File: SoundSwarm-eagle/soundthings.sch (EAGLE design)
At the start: 34 parts, among them Q1 IRLIB9343PbF, Q2 IRLB8721PBF, Q4 IRLB8721PBF

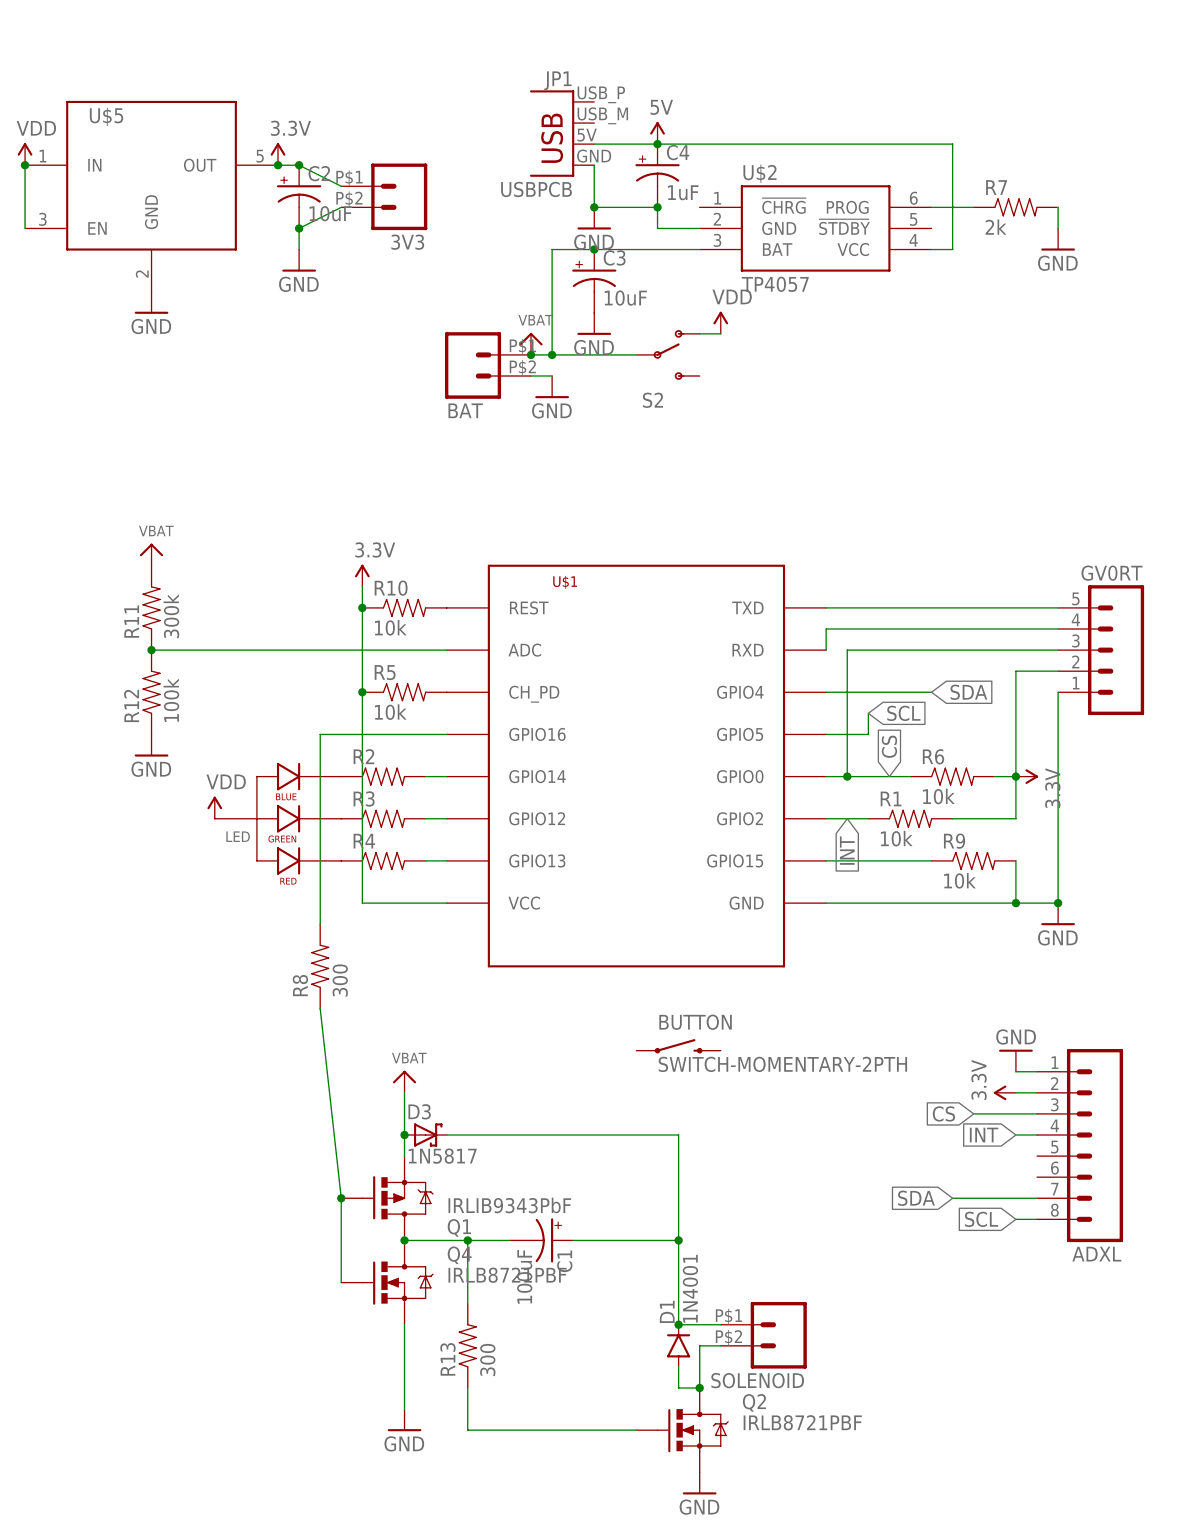
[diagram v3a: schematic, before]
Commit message: New schematic using DC-DC converter; needs Eagle-Lio-Library
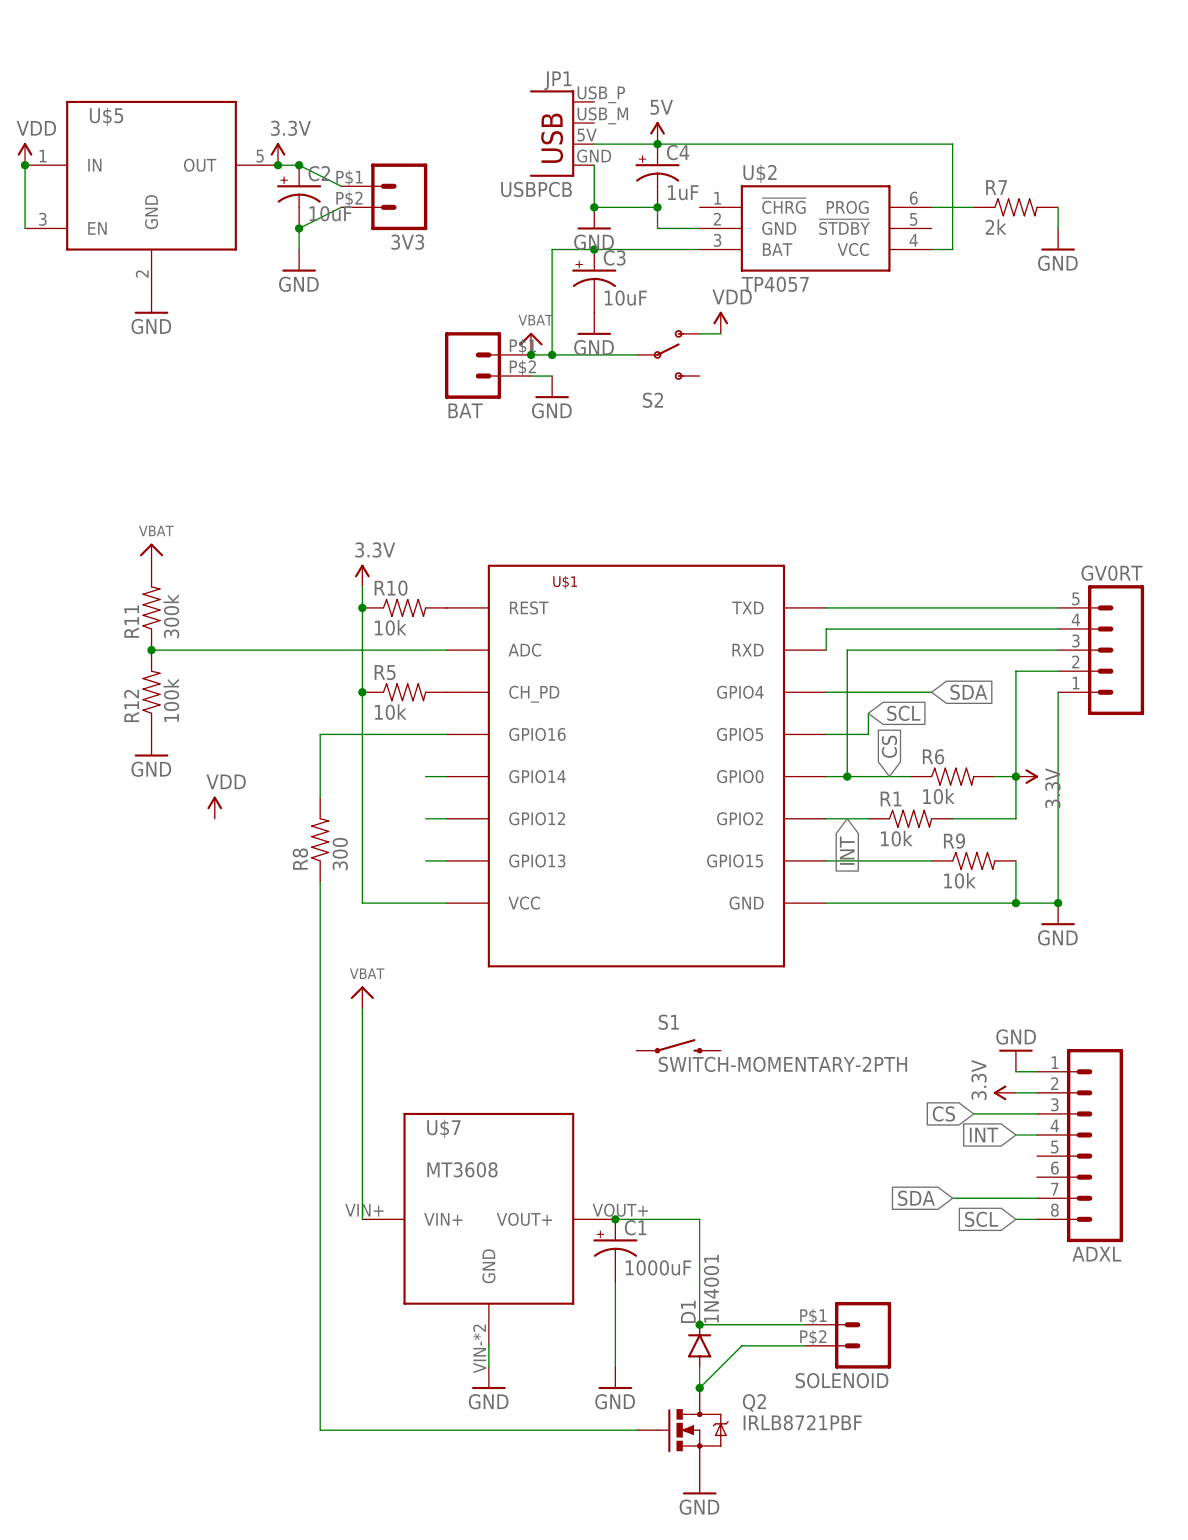
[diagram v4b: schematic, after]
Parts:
- removed D3: 1N5817, adafruit:SCHOTTKY-DIODEDO41
- removed LED: LED-RGB-CA-THRUCLEAR, SparkFun-LED:LED-RGB-CA-THRUCLEAR
- removed Q1: IRLIB9343PbF, SparkFun-DiscreteSemi:MOSFET-PCHANNELFQP27P06
- removed Q4: IRLB8721PBF, SparkFun-DiscreteSemi:MOSFET-NCHANNELFQP30N06L
- removed R13: 300, SparkFun-Passives:RESISTORAXIAL-0.3
- removed R2, R3, R4: (no value), SparkFun-Passives:RESISTORAXIAL-0.3
- added U$7: MT3608, lio:MT3608
- C1: value 100uF -> 1000uF
- renumbered BUTTON to S1
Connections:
- removed net N$12: Q2.G, R13.1
- removed net N$14: LED.RED_CATHODE, R4.1
- removed net N$2: LED.BLUE_CATHODE, R2.1
- removed net N$4: C1.-, Q1.D, Q4.D, R13.2
- removed net N$9: LED.GREEN_CATHODE, R3.1
- removed net VHI: C1.+, D1.C, D3.C, SOLENOID.1
- new net VOUT+: C1.+, D1.C, SOLENOID.1, U$7.VOUT+
- net GATE: now also Q2.G; no longer Q1.G, Q4.G
- net GND: now also C1.-, U$7.GND; no longer Q4.S
- net N$5: no longer R4.2
- net N$6: no longer R3.2
- net N$7: no longer R2.2
- net VBAT: now also U$7.VIN+; no longer D3.A, Q1.S
- net VDD: no longer LED.ANODE
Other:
- moved on the sheet: C1, D1, R8, SOLENOID

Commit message: Fixed PCB layout v2
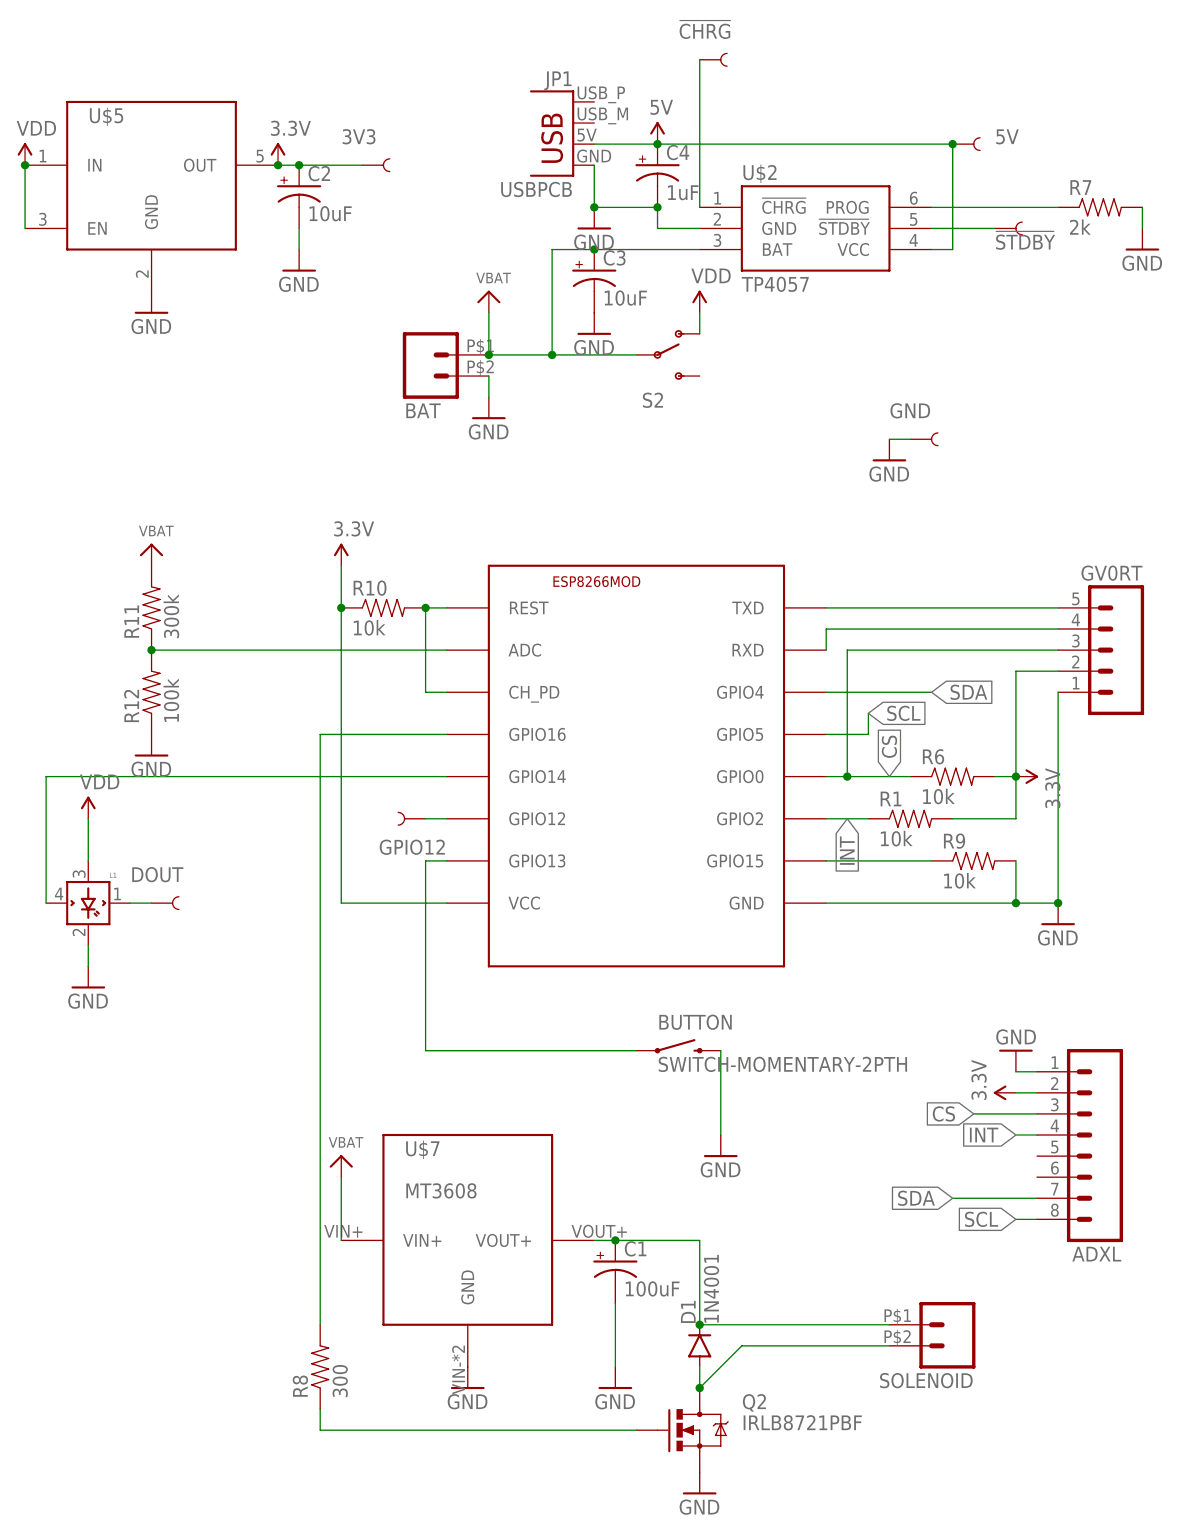
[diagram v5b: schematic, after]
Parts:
- removed R5: 10k, SparkFun-Passives:RESISTORAXIAL-0.3
- added !CHRG, !STDBY, 5V, DOUT, GND, GPIO12: TEST-POINTTP_15TH_THRU, SparkFun-Passives:TEST-POINTTP_15TH_THRU
- added L1: WS2812BTH, lio:WS2812BTH
- 3V3: value (none) -> TEST-POINTTP_15TH_THRU; device SparkFun-Connectors:M02PTH2 -> SparkFun-Passives:TEST-POINTTP_15TH_THRU
- C1: value 1000uF -> 100uF
- renumbered S1 to BUTTON, U$1 to ESP8266MOD
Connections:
- net N$1 renamed SOL-
- net N$15 renamed TX
- net N$16 renamed RX
- net N$19 renamed GPIO15
- removed net N$20: ESP8266MOD.REST, R10.2
- removed net N$5: ESP8266MOD.GPIO13
- removed net N$7: ESP8266MOD.GPIO14
- new net DIN: ESP8266MOD.GPIO14, L1.DIN
- new net DOUT: DOUT.1, L1.DOUT
- new net EN: ESP8266MOD.CH_PD, ESP8266MOD.REST, R10.2
- new net GPIO13: BUTTON.1, ESP8266MOD.GPIO13
- new net N$8: !CHRG.1, U$2.!CHRG
- net 3.3V: no longer R5.1
- net 5V: now also 5V.1
- net GND: now also BUTTON.2, GND.1, L1.GND; no longer 3V3.2
- net N$3: now also !STDBY.1, U$2.!STDBY; no longer ESP8266MOD.CH_PD, R5.2
- net N$6: now also GPIO12.1
- net VDD: now also L1.VDD
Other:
- moved on the sheet: BAT, C1, R10, R7, R8, SOLENOID, U$7

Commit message: Move away from the edges; add labels
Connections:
- net N$3 renamed !STDBY
- net N$6 renamed GPIO12
- net N$8 renamed !CHRG
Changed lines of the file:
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@@
 <grid distance="0.1" unitdist="inch" unit="inch" style="lines" multiple="1" display="no" altdistance="0.01" altunitdist="inch" altunit="inch"/>
 <layers>
-<layer number="1" name="Top" color="4" fill="1" visible="yes" active="no"/>
-<layer number="16" name="Bottom" color="1" fill="1" visible="yes" active="no"/>
-<layer number="17" name="Pads" color="2" fill="1" visible="yes" active="no"/>
-<layer number="18" name="Vias" color="2" fill="1" visible="yes" active="no"/>
-<layer number="19" name="Unrouted" color="6" fill="1" visible="yes" active="no"/>
-<layer number="20" name="Dimension" color="15" fill="1" visible="yes" active="no"/>
-<layer number="21" name="tPlace" color="7" fill="1" visible="yes" active="no"/>
-<layer number="22" name="bPlace" color="7" fill="1" visible="yes" active="no"/>
-<layer number="23" name="tOrigins" color="15" fill="1" visible="yes" active="no"/>
-<layer number="24" name="bOrigins" color="15" fill="1" visible="yes" active="no"/>
-<layer number="25" name="tNames" color="7" fill="1" visible="yes" active="no"/>
-<layer number="26" name="bNames" color="7" fill="1" visible="yes" active="no"/>
-<layer number="27" name="tValues" color="7" fill="1" visible="yes" active="no"/>
-<layer number="28" name="bValues" color="7" fill="1" visible="yes" active="no"/>
+<layer number="1" name="Top" color="4" fill="1" visible="no" active="no"/>
+<layer number="16" name="Bottom" color="1" fill="1" visible="no" active="no"/>
+<layer number="17" name="Pads" color="2" fill="1" visible="no" active="no"/>
+<layer number="18" name="Vias" color="2" fill="1" visible="no" active="no"/>
+<layer number="19" name="Unrouted" color="6" fill="1" visible="no" active="no"/>
+<layer number="20" name="Dimension" color="15" fill="1" visible="no" active="no"/>
+<layer number="21" name="tPlace" color="7" fill="1" visible="no" active="no"/>
+<layer number="22" name="bPlace" color="7" fill="1" visible="no" active="no"/>
+<layer number="23" name="tOrigins" color="15" fill="1" visible="no" active="no"/>
+<layer number="24" name="bOrigins" color="15" fill="1" visible="no" active="no"/>
+<layer number="25" name="tNames" color="7" fill="1" visible="no" active="no"/>
+<layer number="26" name="bNames" color="7" fill="1" visible="no" active="no"/>
+<layer number="27" name="tValues" color="7" fill="1" visible="no" active="no"/>
+<layer number="28" name="bValues" color="7" fill="1" visible="no" active="no"/>
 <layer number="29" name="tStop" color="7" fill="3" visible="no" active="no"/>
 <layer number="30" name="bStop" color="7" fill="6" visible="no" active="no"/>
@@
 <layer number="35" name="tGlue" color="7" fill="4" visible="no" active="no"/>
 <layer number="36" name="bGlue" color="7" fill="5" visible="no" active="no"/>
-<layer number="37" name="tTest" color="7" fill="1" visible="yes" active="no"/>
-<layer number="38" name="bTest" color="7" fill="1" visible="yes" active="no"/>
+<layer number="37" name="tTest" color="7" fill="1" visible="no" active="no"/>
+<layer number="38" name="bTest" color="7" fill="1" visible="no" active="no"/>
 <layer number="39" name="tKeepout" color="4" fill="11" visible="no" active="no"/>
 <layer number="40" name="bKeepout" color="1" fill="11" visible="no" active="no"/>
@@
 <layer number="44" name="Drills" color="7" fill="1" visible="no" active="no"/>
 <layer number="45" name="Holes" color="7" fill="1" visible="no" active="no"/>
-<layer number="46" name="Milling" color="3" fill="1" visible="yes" active="no"/>
-<layer number="47" name="Measures" color="7" fill="1" visible="yes" active="no"/>
-<layer number="48" name="Document" color="7" fill="1" visible="yes" active="no"/>
-<layer number="49" name="Reference" color="7" fill="1" visible="yes" active="no"/>
-<layer number="50" name="dxf" color="7" fill="1" visible="yes" active="no"/>
-<layer number="51" name="tDocu" color="7" fill="1" visible="yes" active="no"/>
-<layer number="52" name="bDocu" color="7" fill="1" visible="yes" active="no"/>
-<layer number="53" name="tGND_GNDA" color="7" fill="9" visible="yes" active="no"/>
-<layer number="54" name="bGND_GNDA" color="1" fill="9" visible="yes" active="no"/>
-<layer number="56" name="wert" color="7" fill="1" visible="yes" active="no"/>
-<layer number="57" name="tCAD" color="7" fill="1" visible="yes" active="no"/>
-<layer number="59" name="tCarbon" color="7" fill="1" visible="yes" active="no"/>
-<layer number="60" name="bCarbon" color="7" fill="1" visible="yes" active="no"/>
+<layer number="46" name="Milling" color="3" fill="1" visible="no" active="no"/>
+<layer number="47" name="Measures" color="7" fill="1" visible="no" active="no"/>
+<layer number="48" name="Document" color="7" fill="1" visible="no" active="no"/>
+<layer number="49" name="Reference" color="7" fill="1" visible="no" active="no"/>
+<layer number="50" name="dxf" color="7" fill="1" visible="no" active="no"/>
+<layer number="51" name="tDocu" color="7" fill="1" visible="no" active="no"/>
+<layer number="52" name="bDocu" color="7" fill="1" visible="no" active="no"/>
+<layer number="53" name="tGND_GNDA" color="7" fill="9" visible="no" active="no"/>
+<layer number="54" name="bGND_GNDA" color="1" fill="9" visible="no" active="no"/>
+<layer number="56" name="wert" color="7" fill="1" visible="no" active="no"/>
+<layer number="57" name="tCAD" color="7" fill="1" visible="no" active="no"/>
+<layer number="59" name="tCarbon" color="7" fill="1" visible="no" active="no"/>
+<layer number="60" name="bCarbon" color="7" fill="1" visible="no" active="no"/>
 <layer number="90" name="Modules" color="5" fill="1" visible="yes" active="yes"/>
 <layer number="91" name="Nets" color="2" fill="1" visible="yes" active="yes"/>
@@
 </segment>
 </net>
-<net name="N$6" class="0">
+<net name="GPIO12" class="0">
 <segment>
 <pinref part="ESP8266MOD" gate="G$1" pin="GPIO12"/>
@@
 </segment>
 </net>
-<net name="N$3" class="0">
+<net name="!STDBY" class="0">
 <segment>
 <pinref part="U$2" gate="G$1" pin="!STDBY"/>
@@
 </segment>
 </net>
-<net name="N$8" class="0">
+<net name="!CHRG" class="0">
 <segment>
 <pinref part="U$2" gate="G$1" pin="!CHRG"/>

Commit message: As submitted to ditrypcbs
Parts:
- renumbered GPIO12 to D6
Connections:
- net DIN renamed GPIO14
- net SCL: now also ESP8266MOD.GPIO4; no longer ESP8266MOD.GPIO5
- net SDA: now also ESP8266MOD.GPIO5; no longer ESP8266MOD.GPIO4
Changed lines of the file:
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@@
 </variantdefs>
 <classes>
-<class number="0" name="default" width="0" drill="0">
+<class number="0" name="default" width="0.2032" drill="0">
+<clearance class="0" value="0.2032"/>
 </class>
 <class number="1" name="ground" width="0.4064" drill="0">
-<clearance class="1" value="0.2032"/>
+<clearance class="1" value="0.3048"/>
 </class>
 <class number="2" name="power" width="0.4064" drill="0">
-<clearance class="2" value="0.2032"/>
+<clearance class="2" value="0.3048"/>
 </class>
 </classes>
@@
 <part name="3V3" library="SparkFun-Passives" deviceset="TEST-POINT" device="TP_15TH_THRU"/>
 <part name="5V" library="SparkFun-Passives" deviceset="TEST-POINT" device="TP_15TH_THRU"/>
-<part name="GPIO12" library="SparkFun-Passives" deviceset="TEST-POINT" device="TP_15TH_THRU"/>
+<part name="D6" library="SparkFun-Passives" deviceset="TEST-POINT" device="TP_15TH_THRU"/>
 <part name="GND" library="SparkFun-Passives" deviceset="TEST-POINT" device="TP_15TH_THRU"/>
 <part name="GND15" library="SparkFun-Aesthetics" deviceset="GND" device=""/>
@@
 <attribute name="NAME" x="106.68" y="175.26" size="1.778" layer="95"/>
 </instance>
-<instance part="GPIO12" gate="G$1" x="38.1" y="93.98" smashed="yes" rot="R180">
+<instance part="D6" gate="G$1" x="38.1" y="93.98" smashed="yes" rot="R180">
 <attribute name="NAME" x="40.64" y="91.44" size="1.778" layer="95" rot="R180"/>
 </instance>
@@
 <pinref part="ESP8266MOD" gate="G$1" pin="GPIO12"/>
 <wire x1="38.1" y1="93.98" x2="40.64" y2="93.98" width="0.1524" layer="91"/>
-<pinref part="GPIO12" gate="G$1" pin="1"/>
-</segment>
-</net>
-<net name="DIN" class="0">
+<pinref part="D6" gate="G$1" pin="1"/>
+</segment>
+</net>
+<net name="GPIO14" class="0">
 <segment>
 <pinref part="ESP8266MOD" gate="G$1" pin="GPIO14"/>
@@
 </segment>
 <segment>
-<pinref part="ESP8266MOD" gate="G$1" pin="GPIO5"/>
+<pinref part="ESP8266MOD" gate="G$1" pin="GPIO4"/>
 <wire x1="86.36" y1="104.14" x2="91.44" y2="104.14" width="0.1524" layer="91"/>
 <wire x1="91.44" y1="104.14" x2="91.44" y2="106.68" width="0.1524" layer="91"/>
@@
 </segment>
 <segment>
-<pinref part="ESP8266MOD" gate="G$1" pin="GPIO4"/>
+<pinref part="ESP8266MOD" gate="G$1" pin="GPIO5"/>
 <wire x1="86.36" y1="109.22" x2="99.06" y2="109.22" width="0.1524" layer="91"/>
 <label x="99.06" y="109.22" size="1.778" layer="95" xref="yes"/>
